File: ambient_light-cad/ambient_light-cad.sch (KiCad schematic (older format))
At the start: 6 parts, among them U1 ATmega328P-AU

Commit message: Add Serial->UART & USB conn
Crystal : 12MHz
IC : CH340G
USB conn : USB-C
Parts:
- removed R? (x2): 1k, symbol Device:R
- added C?: 20nF, symbol Device:C
- added C?: 1uF, symbol Device:C
- added C? (x2): 18pF, symbol Device:C
- added D?: GREEEN, symbol Device:LED
- added D?: RED, symbol Device:LED
- added P?: USB_C_Plug_USB2.0, symbol Connector:USB_C_Plug_USB2.0
- added R? (x2): 1k, symbol Device:R
- added R? (x2): 500, symbol Device:R
- added U?: CH340G, Package_SO:SOIC-16_3.9x9.9mm_P1.27mm, symbol Interface_USB:CH340G
- added Y?: 12MHz, symbol Device:Crystal_GND24
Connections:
- net labels added: +3.3V, +5V, D+, D-, Reset, XI, XO
- wire segments 28 -> 68
- no-connect marks 0 -> 6

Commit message: ICSP,ResetSW
Added ICSP connector, Reset SW circuit
Confirmed circuit between TX and LED
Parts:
- added C?: 100nF, symbol Device:C
- added D?: YELLOW, symbol Device:LED
- added J?: ICSP, symbol Connector_Generic:Conn_02x03_Odd_Even
- added R? (x2): 1k, symbol Device:R
- added SW?: SW_Push, symbol Switch:SW_Push
- P?: symbol Connector:USB_C_Plug_USB2.0 -> ambient_light-cad-rescue:USB_C_Plug_USB2.0-Connector
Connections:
- net labels added: MISO, MOSI, SCK
- wire segments 68 -> 90
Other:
- moved on the sheet: U?

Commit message: Schematic change
changed symbols to small version
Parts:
- removed C?: 20nF, symbol Device:C
- removed C?: 1uF, symbol Device:C
- removed C? (x4): 18pF, symbol Device:C
- removed C?: 100nF, symbol Device:C
- removed D?: GREEEN, symbol Device:LED
- removed D?: RED, symbol Device:LED
- removed D?: YELLOW, symbol Device:LED
- removed R? (x4): 1k, symbol Device:R
- removed R? (x2): 500, symbol Device:R
- removed Y?: 14.4756MHz, symbol Device:Crystal_GND24
- removed Y?: 12MHz, symbol Device:Crystal_GND24
- added C?: 100nF, symbol Device:C_Small
- added C? (x4): 18pF, symbol Device:C_Small
- added C?: 20nF, symbol Device:C_Small
- added C?: 1uF, symbol Device:C_Small
- added D?: Green, symbol Device:LED_Small
- added D?: Yellow, symbol Device:LED_Small
- added D?: Red, symbol Device:LED_Small
- added R? (x4): 1k, symbol Device:R_Small
- added R? (x2): 500, symbol Device:R_Small
- added Y?: 14.4756MHz, symbol Device:Crystal_GND24_Small
- added Y?: 12MHz, symbol Device:Crystal_GND24_Small
- SW?: value SW_Push -> SW_Reset
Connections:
- wire segments 90 -> 96

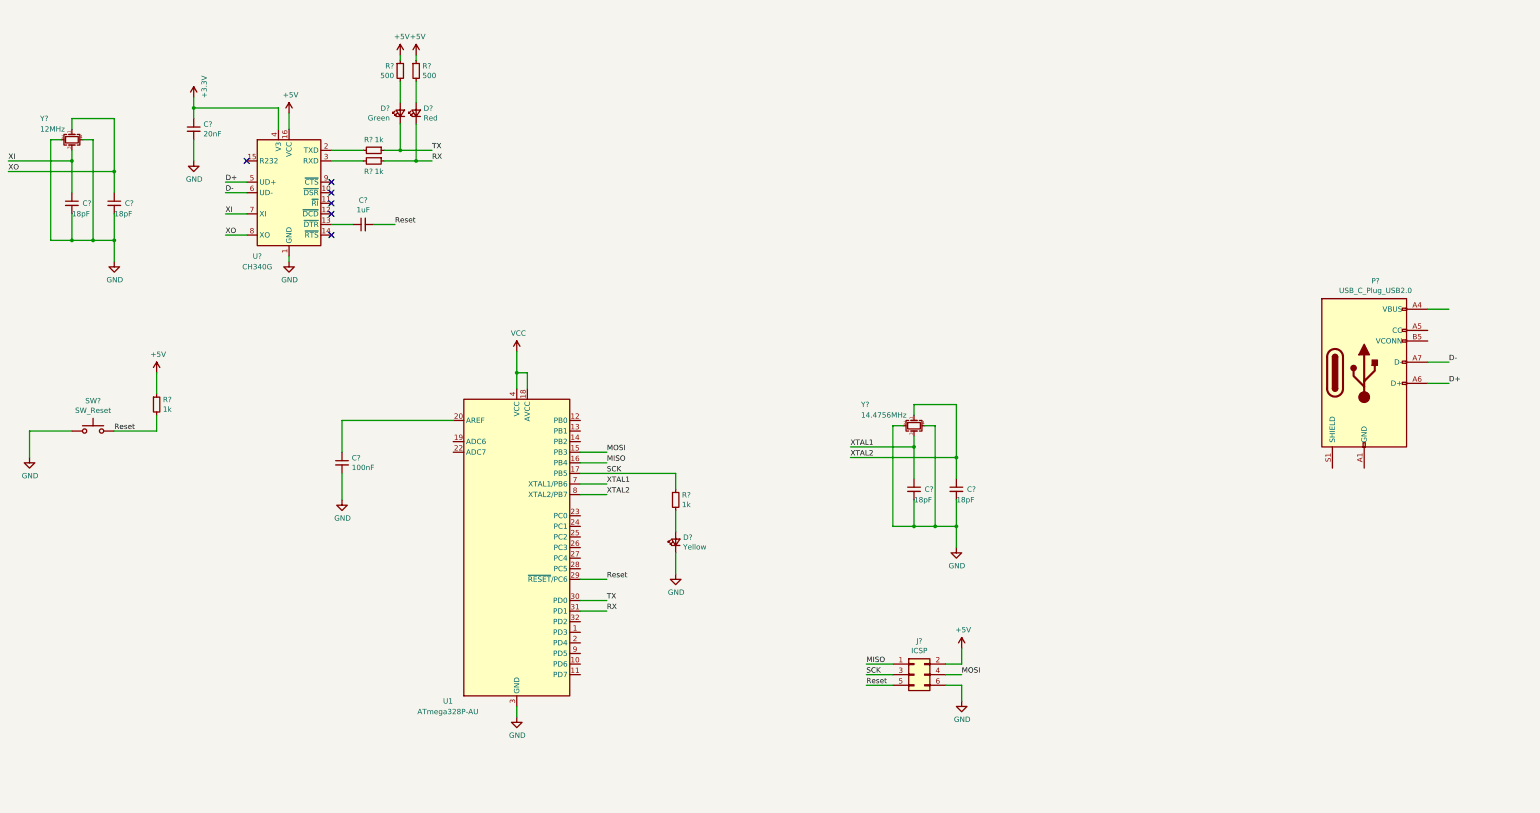
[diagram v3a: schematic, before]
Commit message: [Updated] reset_Sw, led_strip_conn
ATmega328P Reset SW, LED
Neopixel Strip 3pin conn
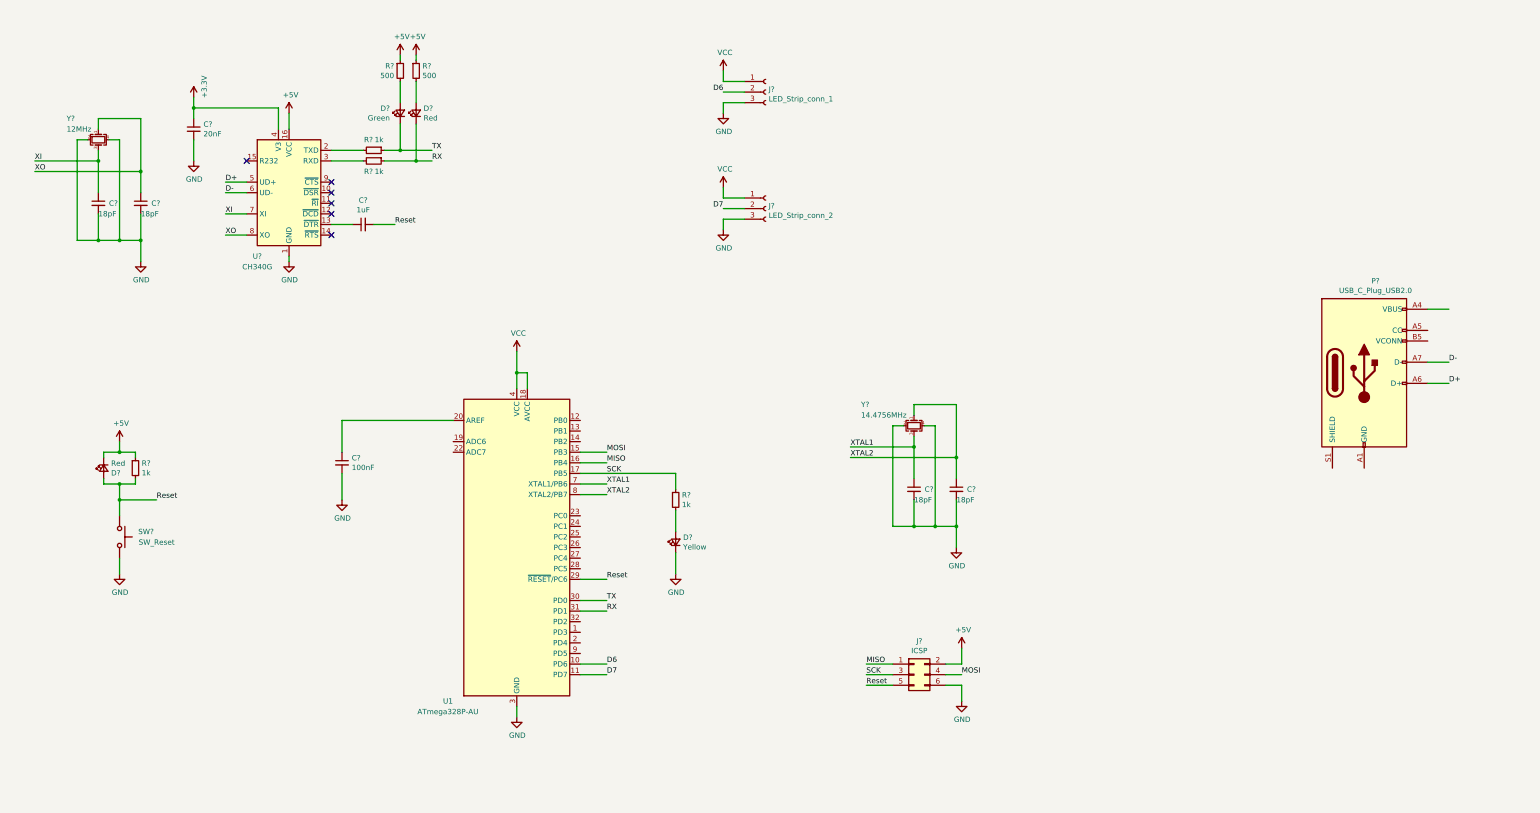
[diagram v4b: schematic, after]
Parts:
- added D?: Red, symbol Device:LED_Small
- added J?: LED_Strip_conn_1, symbol Connector:Conn_01x03_Female
- added J?: LED_Strip_conn_2, symbol Connector:Conn_01x03_Female
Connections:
- net +5V: now also D?.1 (K)
- net GND: now also SW?.2, J?.3 (Pin_3), J?.3 (Pin_3); no longer SW?.1
- net Reset: now also SW?.1, D?.2 (A); no longer SW?.2
- net VCC: now also J?.1 (Pin_1), J?.1 (Pin_1)
- net D6: now reaches U1.10 (PD6)
- net D6: now also J?.2 (Pin_2)
- net D7: now reaches U1.11 (PD7)
- net D7: now also J?.2 (Pin_2)
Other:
- moved on the sheet: C?, R?, SW?, Y?

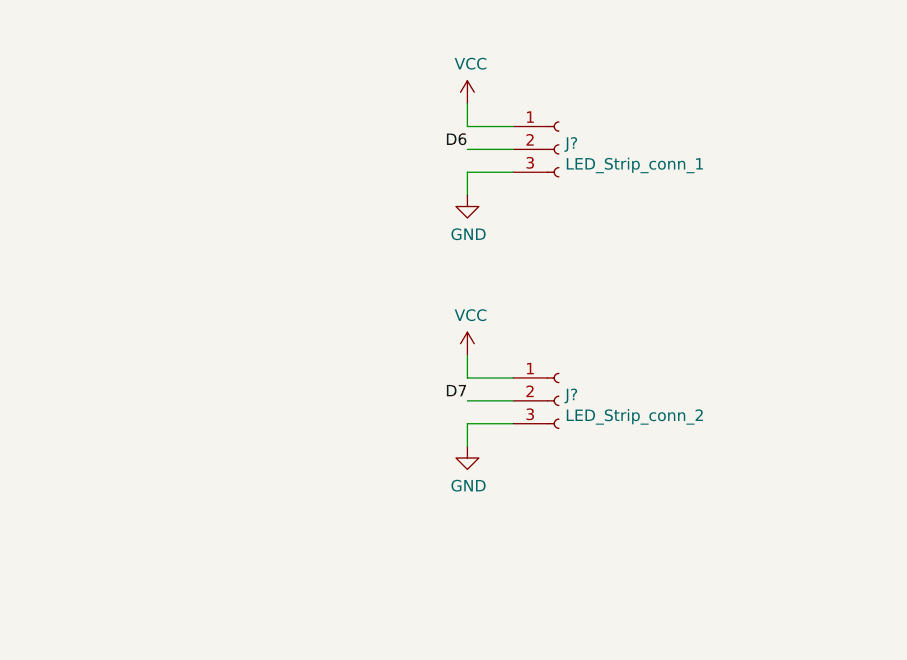
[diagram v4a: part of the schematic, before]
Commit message: [Added] LED_strip Bypass capacitor
220uF * 2
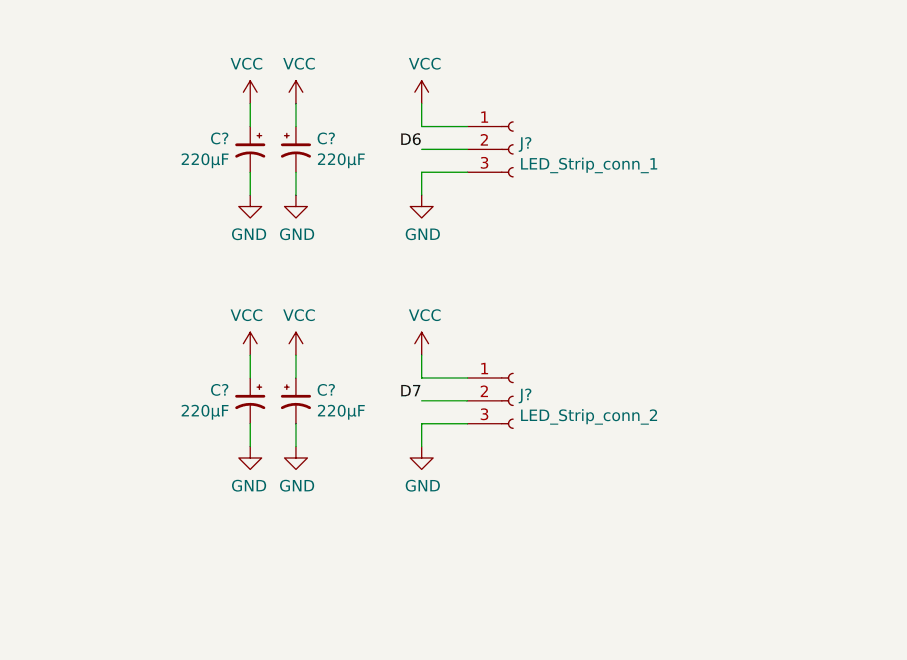
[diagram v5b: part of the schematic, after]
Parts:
- added C? (x4): 220μF, symbol Device:CP1_Small
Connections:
- net GND: now also C?.2, C?.2, C?.2, C?.2
- net VCC: now also C?.1, C?.1, C?.1, C?.1
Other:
- moved on the sheet: J?

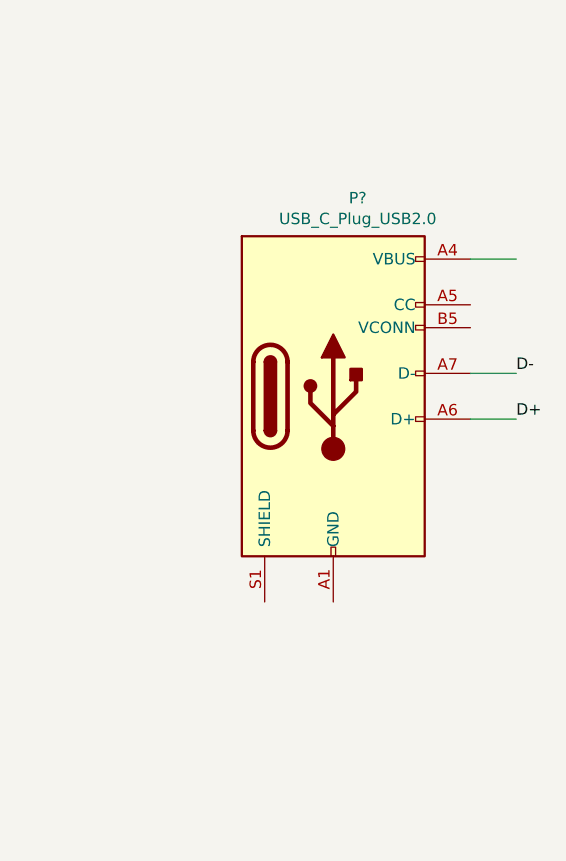
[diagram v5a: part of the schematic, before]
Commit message: [Added] USB type-C conn
USB 2.0 Version.
 D+, D-,  VBUS, GND
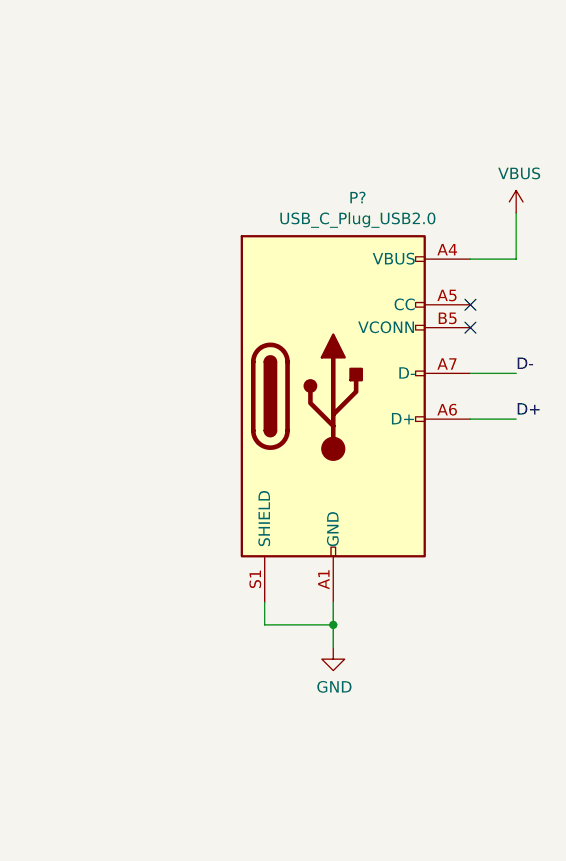
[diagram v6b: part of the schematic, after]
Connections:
- net GND: now also P?.A1 (GND), P?.A12 (GND), P?.B1 (GND), P?.B12 (GND), P?.S1 (SHIELD)
- net VBUS: now reaches P?.A4 (VBUS), P?.A9 (VBUS), P?.B4 (VBUS), P?.B9 (VBUS)
- no-connect marks 6 -> 8
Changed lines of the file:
@@
 	-1   0    0    -1
 $EndComp
+$Comp
+L power:VBUS #PWR?
+U 1 1 5FCFCE9E
+P 14450 3350
+F 0 "#PWR?" H 14450 3200 50  0001 C CNN
+F 1 "VBUS" H 14465 3523 50  0000 C CNN
+F 2 "" H 14450 3350 50  0001 C CNN
+F 3 "" H 14450 3350 50  0001 C CNN
+	1    14450 3350
+	1    0    0    -1
+$EndComp
+Wire Wire Line
+	14450 3350 14450 3550
+NoConn ~ 14250 3750
+NoConn ~ 14250 3850
+$Comp
+L power:GND #PWR?
+U 1 1 5FD0F427
+P 13650 5250
+F 0 "#PWR?" H 13650 5000 50  0001 C CNN
+F 1 "GND" H 13655 5077 50  0000 C CNN
+F 2 "" H 13650 5250 50  0001 C CNN
+F 3 "" H 13650 5250 50  0001 C CNN
+	1    13650 5250
+	1    0    0    -1
+$EndComp
+Wire Wire Line
+	13650 5050 13650 5150
+Wire Wire Line
+	13350 5050 13350 5150
+Wire Wire Line
+	13350 5150 13650 5150
+Connection ~ 13650 5150
+Wire Wire Line
+	13650 5150 13650 5250
 $EndSCHEMATC

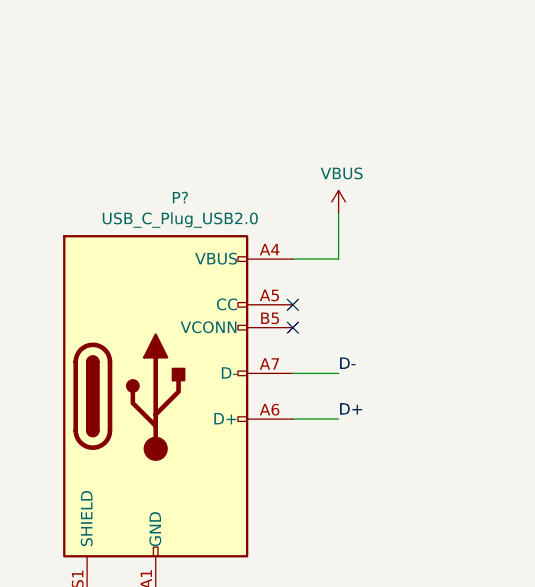
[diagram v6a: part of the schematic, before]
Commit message: [Added] USB type-C conn bypass capacitor
47μF (tantalum capacitor)
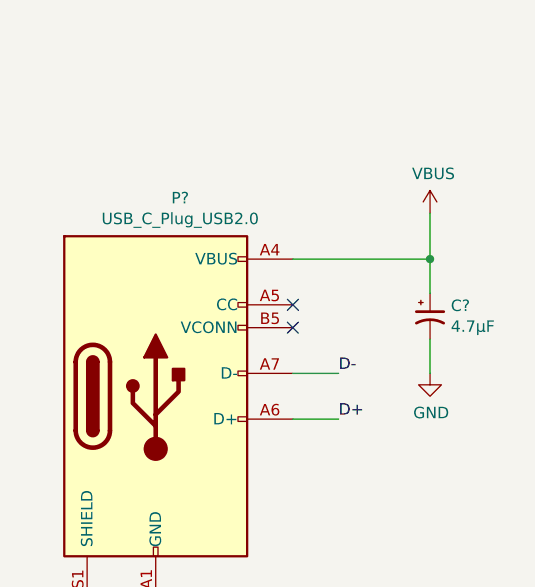
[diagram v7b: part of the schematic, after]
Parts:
- added C?: 4.7μF, symbol Device:CP1_Small
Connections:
- net GND: now also C?.2
- net VBUS: now also C?.1
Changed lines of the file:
@@
-	1    0    0    -1
-$EndComp
-$Comp
-L ambient_light-cad-rescue:USB_C_Plug_USB2.0-Connector P?
-U 1 1 5F7DF33C
-P 13650 4150
-F 0 "P?" H 13757 5017 50  0000 C CNN
-F 1 "USB_C_Plug_USB2.0" H 13757 4926 50  0000 C CNN
-F 2 "" H 13800 4150 50  0001 C CNN
-F 3 "https://www.usb.org/sites/default/files/documents/usb_type-c.zip" H 13800 4150 50  0001 C CNN
-	1    13650 4150
 	1    0    0    -1
 $EndComp
@@
 Text Label 4500 2750 0    50   ~ 0
 Reset
-Wire Wire Line
-	14250 3550 14450 3550
 Wire Wire Line
 	3500 3050 3500 3100
@@
 	-1   0    0    -1
 $EndComp
-$Comp
-L power:VBUS #PWR?
-U 1 1 5FCFCE9E
-P 14450 3350
-F 0 "#PWR?" H 14450 3200 50  0001 C CNN
-F 1 "VBUS" H 14465 3523 50  0000 C CNN
-F 2 "" H 14450 3350 50  0001 C CNN
-F 3 "" H 14450 3350 50  0001 C CNN
-	1    14450 3350
-	1    0    0    -1
-$EndComp
-Wire Wire Line
-	14450 3350 14450 3550
 NoConn ~ 14250 3750
 NoConn ~ 14250 3850
@@
 Wire Wire Line
 	13650 5150 13650 5250
+$Comp
+L ambient_light-cad-rescue:USB_C_Plug_USB2.0-Connector P?
+U 1 1 5F7DF33C
+P 13650 4150
+F 0 "P?" H 13757 5017 50  0000 C CNN
+F 1 "USB_C_Plug_USB2.0" H 13757 4926 50  0000 C CNN
+F 2 "" H 13800 4150 50  0001 C CNN
+F 3 "https://www.usb.org/sites/default/files/documents/usb_type-c.zip" H 13800 4150 50  0001 C CNN
+	1    13650 4150
+	1    0    0    -1
+$EndComp
+$Comp
+L power:GND #PWR?
+U 1 1 5FD2D73E
+P 14850 4050
+F 0 "#PWR?" H 14850 3800 50  0001 C CNN
+F 1 "GND" H 14855 3877 50  0000 C CNN
+F 2 "" H 14850 4050 50  0001 C CNN
+F 3 "" H 14850 4050 50  0001 C CNN
+	1    14850 4050
+	1    0    0    -1
+$EndComp
+Wire Wire Line
+	14850 3350 14850 3550
+$Comp
+L power:VBUS #PWR?
+U 1 1 5FCFCE9E
+P 14850 3350
+F 0 "#PWR?" H 14850 3200 50  0001 C CNN
+F 1 "VBUS" H 14865 3523 50  0000 C CNN
+F 2 "" H 14850 3350 50  0001 C CNN
+F 3 "" H 14850 3350 50  0001 C CNN
+	1    14850 3350
+	1    0    0    -1
+$EndComp
+Wire Wire Line
+	14850 3550 14850 3700
+Connection ~ 14850 3550
+Wire Wire Line
+	14250 3550 14850 3550
+Wire Wire Line
+	14850 3900 14850 4050
+$Comp
+L Device:CP1_Small C?
+U 1 1 5FD787DC
+P 14850 3800
+F 0 "C?" H 14941 3846 50  0000 L CNN
+F 1 "4.7μF" H 14941 3755 50  0000 L CNN
+F 2 "" H 14850 3800 50  0001 C CNN
+F 3 "~" H 14850 3800 50  0001 C CNN
+	1    14850 3800
+	1    0    0    -1
+$EndComp
 $EndSCHEMATC
